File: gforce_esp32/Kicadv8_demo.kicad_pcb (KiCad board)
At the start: 2 copper layers, 455.3 x 164.1 mm, 26 parts, among them J1 USB_C_Receptacle, SW1 TL3215AF160BQ, SW2 TL3215AF160RQ, U1 ESP32-S3-MINI-1U, U2 AP2112K-3.3, U3 LIS3DH

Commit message: gforce_esp32 is newest
added 3d footprint of mcu
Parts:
- removed LED1: ~, B3DQ3BRG_SMT:B3DQ3BRG
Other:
- board size 455.3 x 164.1 mm -> 160 x 160 mm
- copper layers 2 -> 8

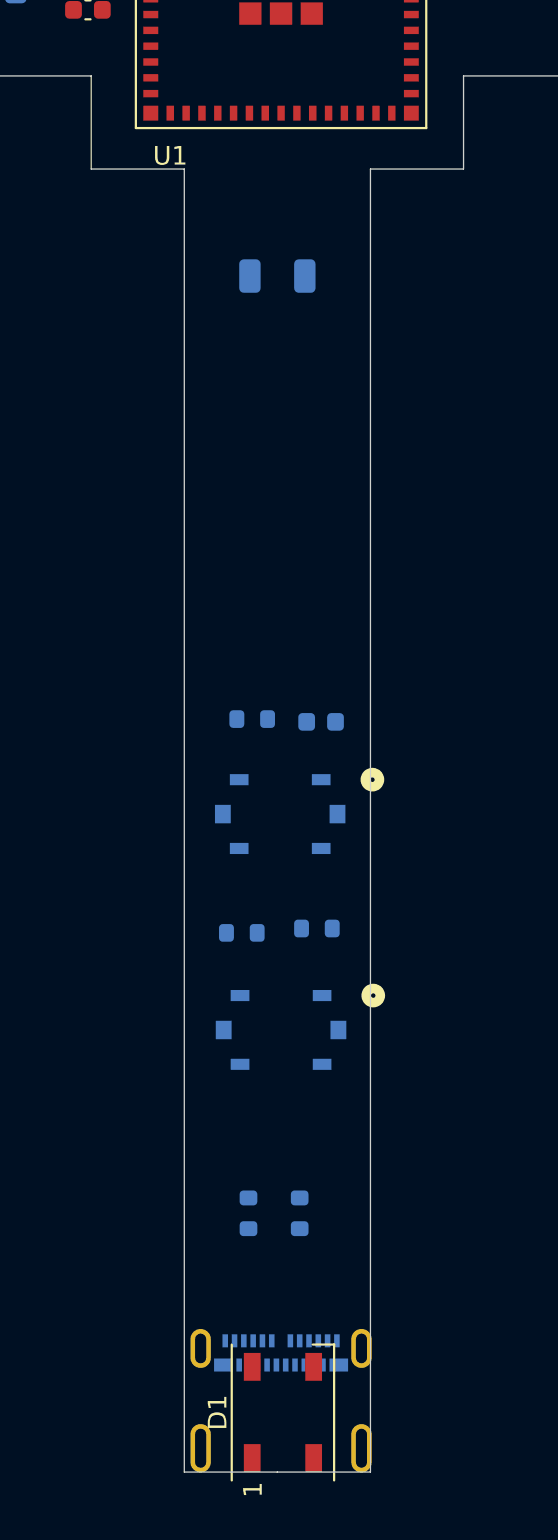
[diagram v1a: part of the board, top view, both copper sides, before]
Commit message: usb diff pair needs updated
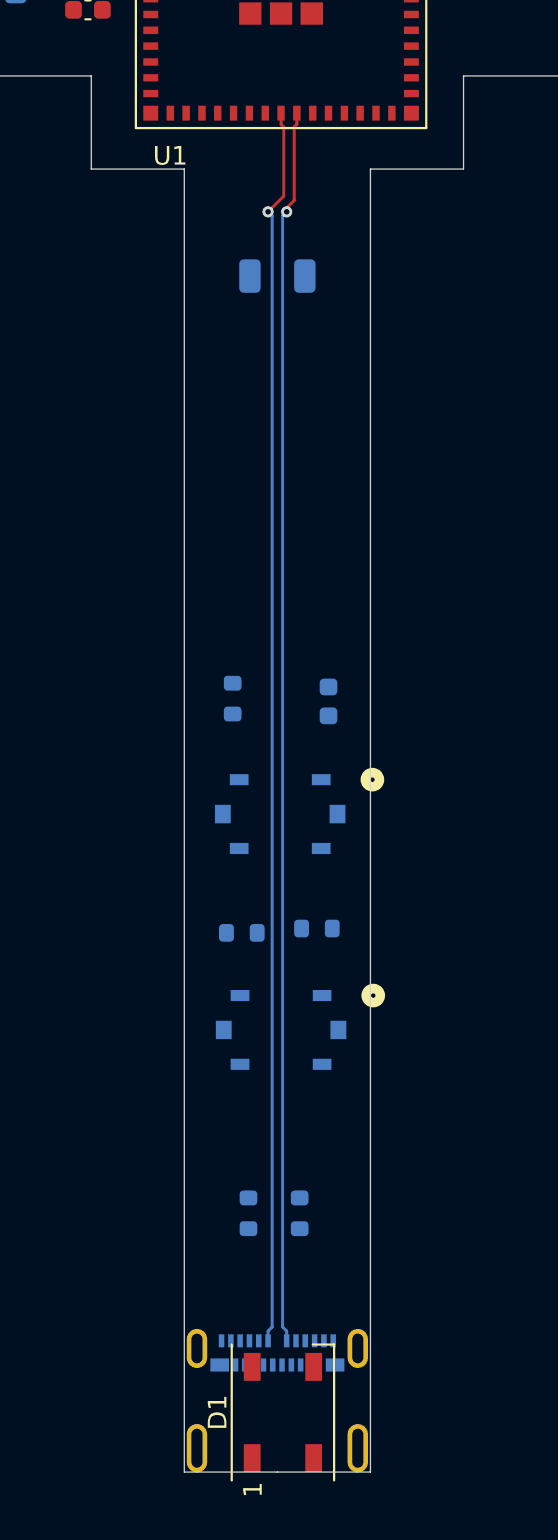
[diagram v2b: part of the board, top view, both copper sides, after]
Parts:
- moved R6 1.52 mm to (142.1, 138.1), turned to -90 degrees
- moved C10 1.17 mm to (147.2, 138.2), turned to -90 degrees
- moved J1 0.20 mm to (144.5, 175.8)
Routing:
- net /D-: track 0.00 -> 66.5 mm, vias 0 -> 1
- net /D+: track 0.00 -> 66.4 mm, vias 0 -> 1
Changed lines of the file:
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@@
 	(footprint "Resistor_SMD:R_0603_1608Metric"
 		(layer "B.Cu")
-		(at 143.1 139.2 180)
+		(at 142.05 138.1 -90)
 		(descr "Resistor SMD 0603 (1608 Metric), square (rectangular) end terminal, IPC_7351 nominal, (Body size source: IPC-SM-782 page 72, https://www.pcb-3d.com/wordpress/wp-content/uploads/ipc-sm-782a_amendment_1_and_2.pdf), generated with kicad-footprint-generator")
 		(tags "resistor")
 		(property "Reference" "R6"
-			(at 0 1.43 180)
+			(at 0 1.43 90)
 			(layer "B.SilkS")
 			(effects
@@
 		)
 		(property "Value" "10K"
-			(at 0 -1.43 180)
+			(at 0 -1.43 90)
 			(layer "B.Fab")
 			(effects
@@
 		)
 		(property "Footprint" "Resistor_SMD:R_0603_1608Metric"
-			(at 0 0 0)
+			(at 0 0 90)
 			(unlocked yes)
 			(layer "B.Fab")
@@
 		)
 		(property "Datasheet" ""
-			(at 0 0 0)
+			(at 0 0 90)
 			(unlocked yes)
 			(layer "B.Fab")
@@
 		)
 		(property "Description" "Resistor"
-			(at 0 0 0)
+			(at 0 0 90)
 			(unlocked yes)
 			(layer "B.Fab")
@@
 		)
 		(fp_line
-			(start 1.48 0.73)
-			(end -1.48 0.73)
+			(start -1.48 0.73)
+			(end -1.48 -0.73)
 			(stroke
 				(width 0.05)
@@
 		)
 		(fp_line
-			(start 1.48 -0.73)
-			(end 1.48 0.73)
+			(start 1.48 0.73)
+			(end -1.48 0.73)
 			(stroke
 				(width 0.05)
@@
 		)
 		(fp_line
-			(start -1.48 0.73)
-			(end -1.48 -0.73)
+			(start -1.48 -0.73)
+			(end 1.48 -0.73)
 			(stroke
 				(width 0.05)
@@
 		)
 		(fp_line
-			(start -1.48 -0.73)
-			(end 1.48 -0.73)
+			(start 1.48 -0.73)
+			(end 1.48 0.73)
 			(stroke
 				(width 0.05)
@@
 		)
 		(fp_line
-			(start 0.8 0.4125)
-			(end -0.8 0.4125)
+			(start -0.8 0.4125)
+			(end -0.8 -0.4125)
 			(stroke
 				(width 0.1)
@@
 		)
 		(fp_line
-			(start 0.8 -0.4125)
-			(end 0.8 0.4125)
+			(start 0.8 0.4125)
+			(end -0.8 0.4125)
 			(stroke
 				(width 0.1)
@@
 		)
 		(fp_line
-			(start -0.8 0.4125)
-			(end -0.8 -0.4125)
+			(start -0.8 -0.4125)
+			(end 0.8 -0.4125)
 			(stroke
 				(width 0.1)
@@
 		)
 		(fp_line
-			(start -0.8 -0.4125)
-			(end 0.8 -0.4125)
+			(start 0.8 -0.4125)
+			(end 0.8 0.4125)
 			(stroke
 				(width 0.1)
@@
 		)
 		(fp_text user "${REFERENCE}"
-			(at 0 0 180)
+			(at 0 0 90)
 			(layer "B.Fab")
 			(effects
@@
 		)
 		(pad "1" smd roundrect
-			(at -0.825 0 180)
+			(at -0.825 0 270)
 			(size 0.8 0.95)
 			(layers "B.Cu" "B.Paste" "B.Mask")
@@
 		)
 		(pad "2" smd roundrect
-			(at 0.825 0 180)
+			(at 0.825 0 270)
 			(size 0.8 0.95)
 			(layers "B.Cu" "B.Paste" "B.Mask")
@@
 	(footprint "Connector_USB:USB_C_Receptacle_Molex_105450-0101"
 		(layer "B.Cu")
-		(at 144.65 175.815 180)
+		(at 144.452 175.815 180)
 		(descr "USB 3.0 3.1 3.2 4.0 Type-C receptable, through-hole mount, SMD, right-angle (https://www.molex.com/pdm_docs/sd/1054500101_sd.pdf)")
 		(tags "USB C Type-C USB3 receptacle SMD")
@@
 			(polygon
 				(pts
-					(xy 141.15 180.14) (xy 148.15 180.14) (xy 148.15 174.51) (xy 141.15 174.51)
+					(xy 140.952 180.14) (xy 147.952 180.14) (xy 147.952 174.51) (xy 140.952 174.51)
 				)
 			)
 		)
-		(model "${KICAD8_3DMODEL_DIR}/Connector_USB.3dshapes/USB_C_Receptacle_Molex_105450-0101.wrl"
+		(model "${KICAD8_3DMODEL_DIR}/Connector_USB.3dshapes/USB_C_Receptacle_GCT_USB4125-xx-x-0190_6P_TopMnt_Horizontal.wrl"
 			(offset
 				(xyz 0 0 0)
@@
 	(footprint "Capacitor_SMD:C_0603_1608Metric"
 		(layer "B.Cu")
-		(at 146.8 139.35 180)
+		(at 147.2 138.25 -90)
 		(descr "Capacitor SMD 0603 (1608 Metric), square (rectangular) end terminal, IPC_7351 nominal, (Body size source: IPC-SM-782 page 76, https://www.pcb-3d.com/wordpress/wp-content/uploads/ipc-sm-782a_amendment_1_and_2.pdf), generated with kicad-footprint-generator")
 		(tags "capacitor")
 		(property "Reference" "C10"
-			(at 0 1.43 180)
+			(at 0 1.43 90)
 			(layer "B.SilkS")
 			(effects
@@
 		)
 		(property "Value" "1uF"
-			(at 0 -1.43 180)
+			(at 0 -1.43 90)
 			(layer "B.Fab")
 			(effects
@@
 		)
 		(property "Footprint" "Capacitor_SMD:C_0603_1608Metric"
-			(at 0 0 0)
+			(at 0 0 90)
 			(unlocked yes)
 			(layer "B.Fab")
@@
 		)
 		(property "Datasheet" "https://www.digikey.com/en/products/detail/murata-electronics/GCM188R71C105KA64D/1979250"
-			(at 0 0 0)
+			(at 0 0 90)
 			(unlocked yes)
 			(layer "B.Fab")
@@
 		)
 		(property "Description" "Unpolarized capacitor"
-			(at 0 0 0)
+			(at 0 0 90)
 			(unlocked yes)
 			(layer "B.Fab")
@@
 		)
 		(fp_line
-			(start 1.48 0.73)
-			(end -1.48 0.73)
+			(start -1.48 0.73)
+			(end -1.48 -0.73)
 			(stroke
 				(width 0.05)
@@
 		)
 		(fp_line
-			(start 1.48 -0.73)
-			(end 1.48 0.73)
+			(start 1.48 0.73)
+			(end -1.48 0.73)
 			(stroke
 				(width 0.05)
@@
 		)
 		(fp_line
-			(start -1.48 0.73)
-			(end -1.48 -0.73)
+			(start -1.48 -0.73)
+			(end 1.48 -0.73)
 			(stroke
 				(width 0.05)
@@
 		)
 		(fp_line
-			(start -1.48 -0.73)
-			(end 1.48 -0.73)
+			(start 1.48 -0.73)
+			(end 1.48 0.73)
 			(stroke
 				(width 0.05)
@@
 		)
 		(fp_line
-			(start 0.8 0.4)
-			(end -0.8 0.4)
+			(start -0.8 0.4)
+			(end -0.8 -0.4)
 			(stroke
 				(width 0.1)
@@
 		)
 		(fp_line
-			(start 0.8 -0.4)
-			(end 0.8 0.4)
+			(start 0.8 0.4)
+			(end -0.8 0.4)
 			(stroke
 				(width 0.1)
@@
 		)
 		(fp_line
-			(start -0.8 0.4)
-			(end -0.8 -0.4)
+			(start -0.8 -0.4)
+			(end 0.8 -0.4)
 			(stroke
 				(width 0.1)
@@
 		)
 		(fp_line
-			(start -0.8 -0.4)
-			(end 0.8 -0.4)
+			(start 0.8 -0.4)
+			(end 0.8 0.4)
 			(stroke
 				(width 0.1)
@@
 		)
 		(fp_text user "${REFERENCE}"
-			(at 0 0 180)
+			(at 0 0 90)
 			(layer "B.Fab")
 			(effects
@@
 		)
 		(pad "1" smd roundrect
-			(at -0.775 0 180)
+			(at -0.775 0 270)
 			(size 0.9 0.95)
 			(layers "B.Cu" "B.Paste" "B.Mask")
@@
 		)
 		(pad "2" smd roundrect
-			(at 0.775 0 180)
+			(at 0.775 0 270)
 			(size 0.9 0.95)
 			(layers "B.Cu" "B.Paste" "B.Mask")
@@
 		(layer "Edge.Cuts")
 	)
+	(segment
+		(start 145.355 111.33896)
+		(end 145.355 107.395001)
+		(width 0.16)
+		(layer "F.Cu")
+		(net 54)
+	)
+	(segment
+		(start 144.952 111.74196)
+		(end 145.355 111.33896)
+		(width 0.16)
+		(layer "F.Cu")
+		(net 54)
+	)
+	(segment
+		(start 144.952 111.95)
+		(end 144.952 111.74196)
+		(width 0.16)
+		(layer "F.Cu")
+		(net 54)
+	)
+	(segment
+		(start 145.355 107.395001)
+		(end 145.5 107.250001)
+		(width 0.16)
+		(layer "F.Cu")
+		(net 54)
+	)
+	(segment
+		(start 145.5 107.250001)
+		(end 145.5 106.65)
+		(width 0.16)
+		(layer "F.Cu")
+		(net 54)
+	)
+	(via
+		(at 144.952 111.95)
+		(size 0.6)
+		(drill 0.3)
+		(layers "F.Cu" "B.Cu")
+		(net 54)
+	)
+	(segment
+		(start 144.952 172.6)
+		(end 144.952 172.074999)
+		(width 0.16)
+		(layer "B.Cu")
+		(net 54)
+	)
+	(segment
+		(start 144.952 172.074999)
+		(end 144.732 171.854999)
+		(width 0.16)
+		(layer "B.Cu")
+		(net 54)
+	)
+	(segment
+		(start 144.732 171.854999)
+		(end 144.732 112.17)
+		(width 0.16)
+		(layer "B.Cu")
+		(net 54)
+	)
+	(segment
+		(start 144.732 112.17)
+		(end 144.952 111.95)
+		(width 0.16)
+		(layer "B.Cu")
+		(net 54)
+	)
+	(segment
+		(start 144.65 107.250001)
+		(end 144.65 106.65)
+		(width 0.16)
+		(layer "F.Cu")
+		(net 55)
+	)
+	(segment
+		(start 144.795 111.107)
+		(end 144.795 107.395001)
+		(width 0.16)
+		(layer "F.Cu")
+		(net 55)
+	)
+	(segment
+		(start 144.795 107.395001)
+		(end 144.65 107.250001)
+		(width 0.16)
+		(layer "F.Cu")
+		(net 55)
+	)
+	(segment
+		(start 143.952 111.95)
+		(end 144.795 111.107)
+		(width 0.16)
+		(layer "F.Cu")
+		(net 55)
+	)
+	(via
+		(at 143.952 111.95)
+		(size 0.6)
+		(drill 0.3)
+		(layers "F.Cu" "B.Cu")
+		(net 55)
+	)
+	(segment
+		(start 144.172 112.17)
+		(end 143.952 111.95)
+		(width 0.16)
+		(layer "B.Cu")
+		(net 55)
+	)
+	(segment
+		(start 143.952 172.6)
+		(end 143.952 172.074999)
+		(width 0.16)
+		(layer "B.Cu")
+		(net 55)
+	)
+	(segment
+		(start 143.952 172.074999)
+		(end 144.172 171.854999)
+		(width 0.16)
+		(layer "B.Cu")
+		(net 55)
+	)
+	(segment
+		(start 144.172 171.854999)
+		(end 144.172 112.17)
+		(width 0.16)
+		(layer "B.Cu")
+		(net 55)
+	)
 	(group ""

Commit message: layout placing parts
lined up leds
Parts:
- added D10: WS2812B, LED_SMD:LED_WS2812B_PLCC4_5.0x5.0mm_P3.2mm, F.Cu at (144.4, 23.8)
- added D11: WS2812B, LED_SMD:LED_WS2812B_PLCC4_5.0x5.0mm_P3.2mm, F.Cu at (158.6, 99.7)
- added D12: WS2812B, LED_SMD:LED_WS2812B_PLCC4_5.0x5.0mm_P3.2mm, F.Cu at (165.3, 99.7)
- added D13: WS2812B, LED_SMD:LED_WS2812B_PLCC4_5.0x5.0mm_P3.2mm, F.Cu at (171.9, 99.7)
- added D14: WS2812B, LED_SMD:LED_WS2812B_PLCC4_5.0x5.0mm_P3.2mm, F.Cu at (178.6, 99.7)
- added D15: WS2812B, LED_SMD:LED_WS2812B_PLCC4_5.0x5.0mm_P3.2mm, F.Cu at (185.2, 99.7)
- added D16: WS2812B, LED_SMD:LED_WS2812B_PLCC4_5.0x5.0mm_P3.2mm, F.Cu at (191.9, 99.7)
- added D17: WS2812B, LED_SMD:LED_WS2812B_PLCC4_5.0x5.0mm_P3.2mm, F.Cu at (198.6, 99.7)
- added D18: WS2812B, LED_SMD:LED_WS2812B_PLCC4_5.0x5.0mm_P3.2mm, F.Cu at (205.2, 99.7)
- added D19: WS2812B, LED_SMD:LED_WS2812B_PLCC4_5.0x5.0mm_P3.2mm, F.Cu at (211.9, 99.7)
- added D2: WS2812B, LED_SMD:LED_WS2812B_PLCC4_5.0x5.0mm_P3.2mm, F.Cu at (144.5, 76.4)
- added D20: WS2812B, LED_SMD:LED_WS2812B_PLCC4_5.0x5.0mm_P3.2mm, F.Cu at (218.6, 99.7)
- added D21: WS2812B, LED_SMD:LED_WS2812B_PLCC4_5.0x5.0mm_P3.2mm, F.Cu at (144.5, 113.0)
- added D22: WS2812B, LED_SMD:LED_WS2812B_PLCC4_5.0x5.0mm_P3.2mm, F.Cu at (144.5, 119.8)
- added D23: WS2812B, LED_SMD:LED_WS2812B_PLCC4_5.0x5.0mm_P3.2mm, F.Cu at (144.5, 126.5)
- added D24: WS2812B, LED_SMD:LED_WS2812B_PLCC4_5.0x5.0mm_P3.2mm, F.Cu at (144.5, 133.2)
- added D25: WS2812B, LED_SMD:LED_WS2812B_PLCC4_5.0x5.0mm_P3.2mm, F.Cu at (144.5, 139.9)
- added D26: WS2812B, LED_SMD:LED_WS2812B_PLCC4_5.0x5.0mm_P3.2mm, F.Cu at (144.5, 146.7)
- added D27: WS2812B, LED_SMD:LED_WS2812B_PLCC4_5.0x5.0mm_P3.2mm, F.Cu at (144.5, 153.4)
- added D28: WS2812B, LED_SMD:LED_WS2812B_PLCC4_5.0x5.0mm_P3.2mm, F.Cu at (144.5, 160.1)
- added D29: WS2812B, LED_SMD:LED_WS2812B_PLCC4_5.0x5.0mm_P3.2mm, F.Cu at (144.5, 166.9)
- added D3: WS2812B, LED_SMD:LED_WS2812B_PLCC4_5.0x5.0mm_P3.2mm, F.Cu at (144.5, 69.8)
- added D30: WS2812B, LED_SMD:LED_WS2812B_PLCC4_5.0x5.0mm_P3.2mm, F.Cu at (144.5, 173.6)
- added D31: WS2812B, LED_SMD:LED_WS2812B_PLCC4_5.0x5.0mm_P3.2mm, F.Cu at (129.2, 99.7)
- added D32: WS2812B, LED_SMD:LED_WS2812B_PLCC4_5.0x5.0mm_P3.2mm, F.Cu at (122.4, 99.7)
- added D33: WS2812B, LED_SMD:LED_WS2812B_PLCC4_5.0x5.0mm_P3.2mm, F.Cu at (115.6, 99.7)
- added D34: WS2812B, LED_SMD:LED_WS2812B_PLCC4_5.0x5.0mm_P3.2mm, F.Cu at (108.8, 99.7)
- added D35: WS2812B, LED_SMD:LED_WS2812B_PLCC4_5.0x5.0mm_P3.2mm, F.Cu at (102.0, 99.7)
- added D36: WS2812B, LED_SMD:LED_WS2812B_PLCC4_5.0x5.0mm_P3.2mm, F.Cu at (95.1, 99.7)
- added D37: WS2812B, LED_SMD:LED_WS2812B_PLCC4_5.0x5.0mm_P3.2mm, F.Cu at (88.3, 99.7)
- added D38: WS2812B, LED_SMD:LED_WS2812B_PLCC4_5.0x5.0mm_P3.2mm, F.Cu at (81.5, 99.7)
- added D39: WS2812B, LED_SMD:LED_WS2812B_PLCC4_5.0x5.0mm_P3.2mm, F.Cu at (74.7, 99.7)
- added D4: WS2812B, LED_SMD:LED_WS2812B_PLCC4_5.0x5.0mm_P3.2mm, F.Cu at (144.5, 63.2)
- added D40: WS2812B, LED_SMD:LED_WS2812B_PLCC4_5.0x5.0mm_P3.2mm, F.Cu at (67.9, 99.7)
- added D5: WS2812B, LED_SMD:LED_WS2812B_PLCC4_5.0x5.0mm_P3.2mm, F.Cu at (144.5, 56.5)
- added D6: WS2812B, LED_SMD:LED_WS2812B_PLCC4_5.0x5.0mm_P3.2mm, F.Cu at (144.5, 49.9)
- added D7: WS2812B, LED_SMD:LED_WS2812B_PLCC4_5.0x5.0mm_P3.2mm, F.Cu at (144.5, 43.3)
- added D8: WS2812B, LED_SMD:LED_WS2812B_PLCC4_5.0x5.0mm_P3.2mm, F.Cu at (144.5, 36.7)
- added D9: WS2812B, LED_SMD:LED_WS2812B_PLCC4_5.0x5.0mm_P3.2mm, F.Cu at (144.5, 30.1)
- added LED1: ~, B3DQ3BRG_SMT:B3DQ3BRG, F.Cu at (259.7, 37.9)
- moved D1 93.5 mm to (144.5, 83.0), turned to 180 degrees
- moved C11 0.73 mm to (134.6, 100.5)
- moved C9 0.73 mm to (134.6, 98.0)
